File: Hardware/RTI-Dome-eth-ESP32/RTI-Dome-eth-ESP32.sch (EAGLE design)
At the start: 96 parts, among them IC1 LM2675MX-5.0_NOPB, IC2 24LC64T-I/SN, IC8 REG1117-3.3V, J1 691313510003, J10 691313510002, J11 691313510002, J12 691313510002, J2 XT60PW-M, J3 691313510003, J4 691313510003, J6 691313510003, J7 691313510003, J8 691313510002, J9 691313510002, T1 MMBT3904LT1, T2 MMBT3904LT1, T3 MMBT3904LT1, U1 W5500, U2 ESP32-DevKitC-32UE, X9 J1011F01PNL

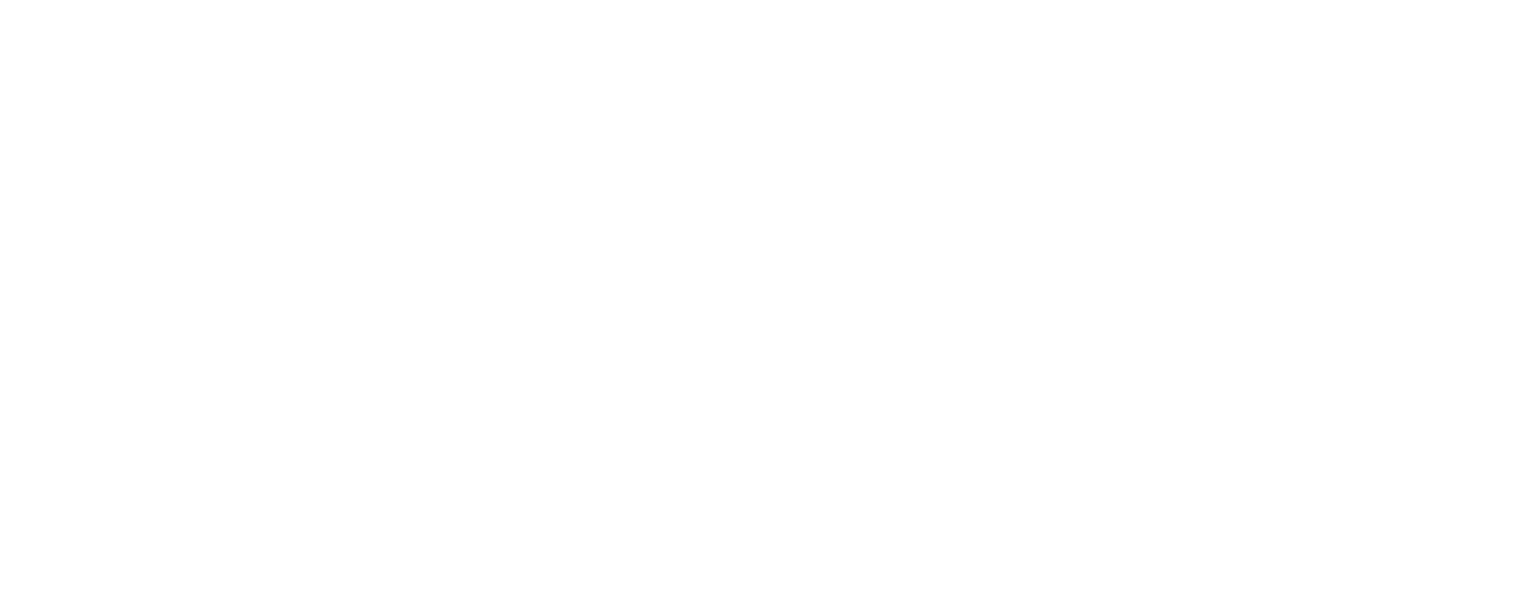
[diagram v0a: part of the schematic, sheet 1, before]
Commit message: Changing 5V circuit
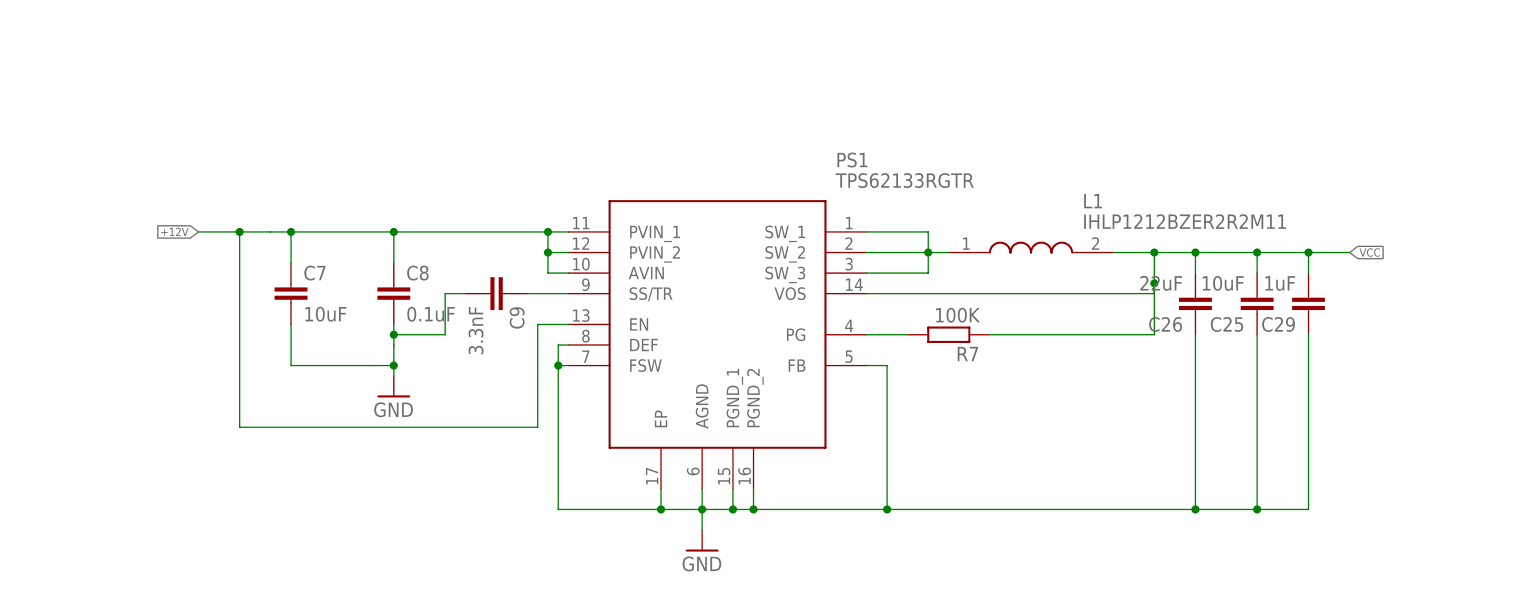
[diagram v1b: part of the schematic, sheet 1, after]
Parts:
- added C25: 10uF, rcl:C-EUC0805
- added C26: 22uF, rcl:C-EUC0805
- added C29: 1uF, rcl:C-EUC0805
- added C7: 10uF, rcl:C-EUC1206
- added C8: 0.1uF, rcl:C-EUC1206
- added C9: 3.3nF, rcl:C-EUC0805
- added L1: IHLP1212BZER2R2M11, samacsys:IHLP1212BZER2R2M11
- added PS1: TPS62133RGTR, samacsys:TPS62133RGTR
- added R7: 100K, rcl:R-EU_R0603
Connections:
- new net PG: PS1.PG, R7.2
- new net SS/TR: C9.1, PS1.SS/TR
- new net SW: L1.1, PS1.SW_1, PS1.SW_2, PS1.SW_3
- net +12V: now also C7.1, C8.1, PS1.AVIN, PS1.EN, PS1.PVIN_1, PS1.PVIN_2
- net GND: now also C25.1, C26.1, C29.1, C7.2, C8.2, C9.2, PS1.AGND, PS1.DEF, PS1.EP, PS1.FB, PS1.FSW, PS1.PGND_1, PS1.PGND_2
- net VCC: now also C25.2, C26.2, C29.2, L1.2, PS1.VOS, R7.1

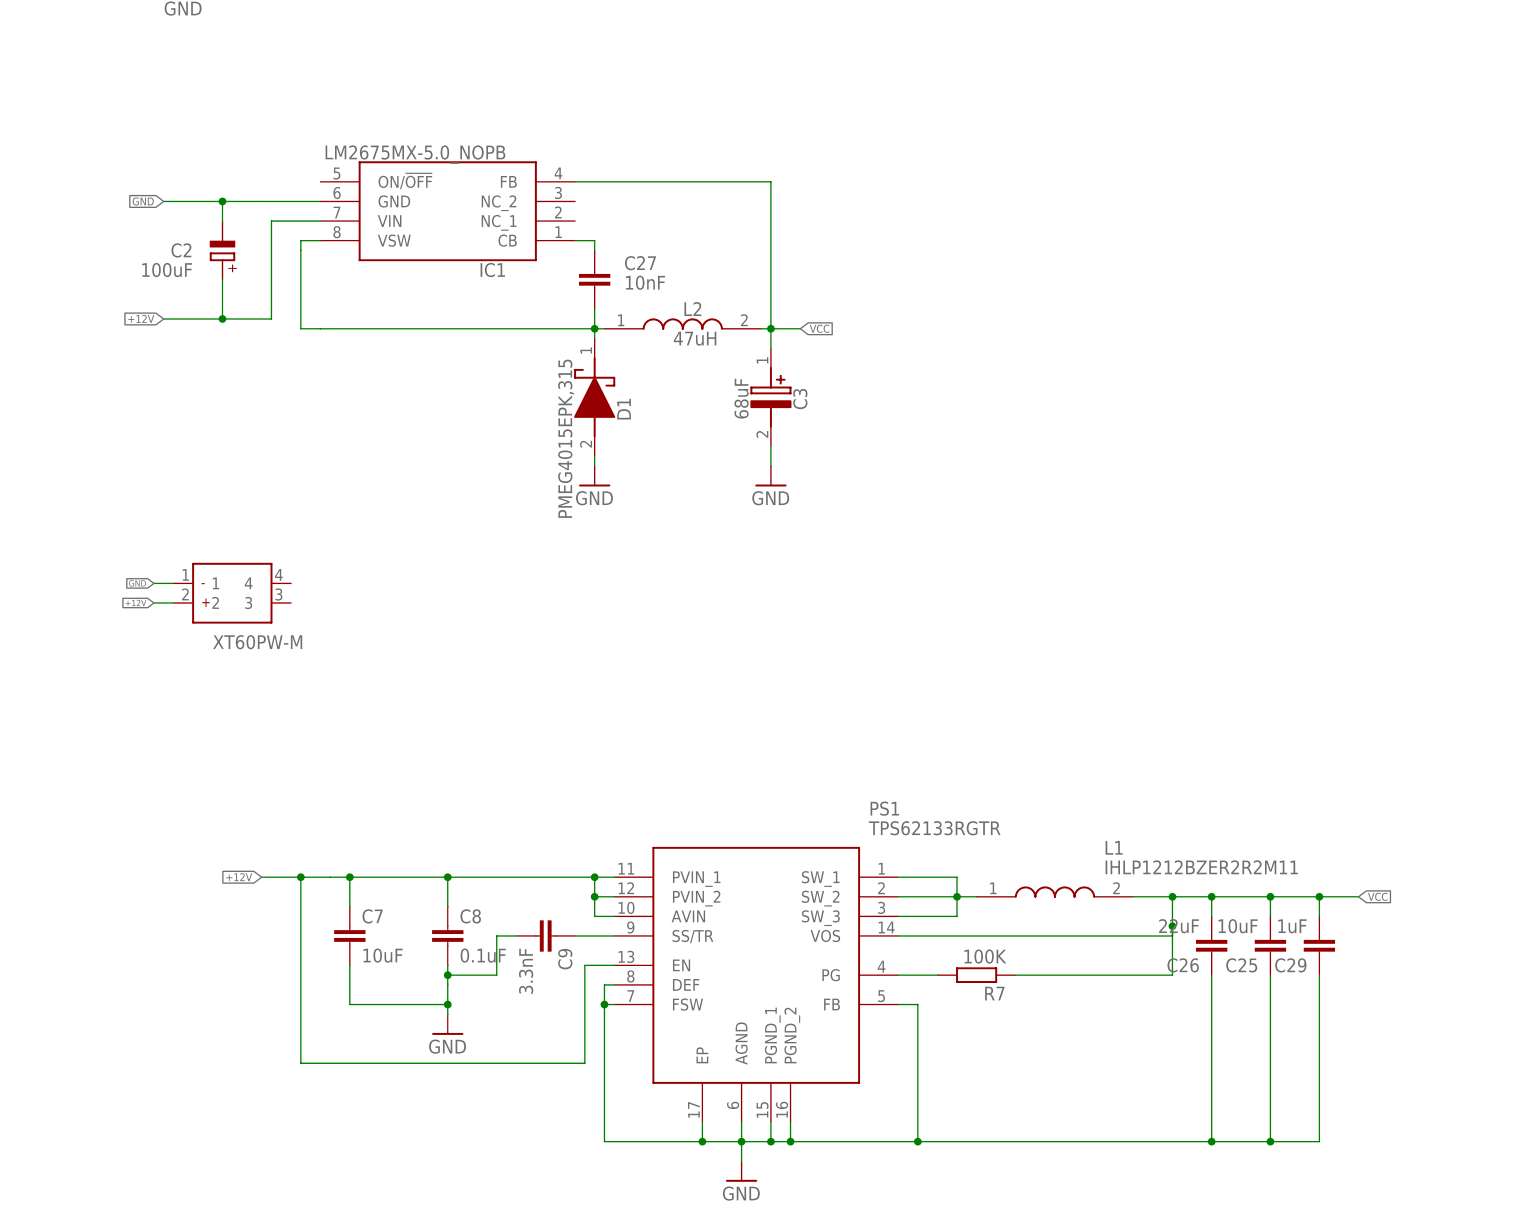
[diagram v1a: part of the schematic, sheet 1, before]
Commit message: New 5V circuit routed
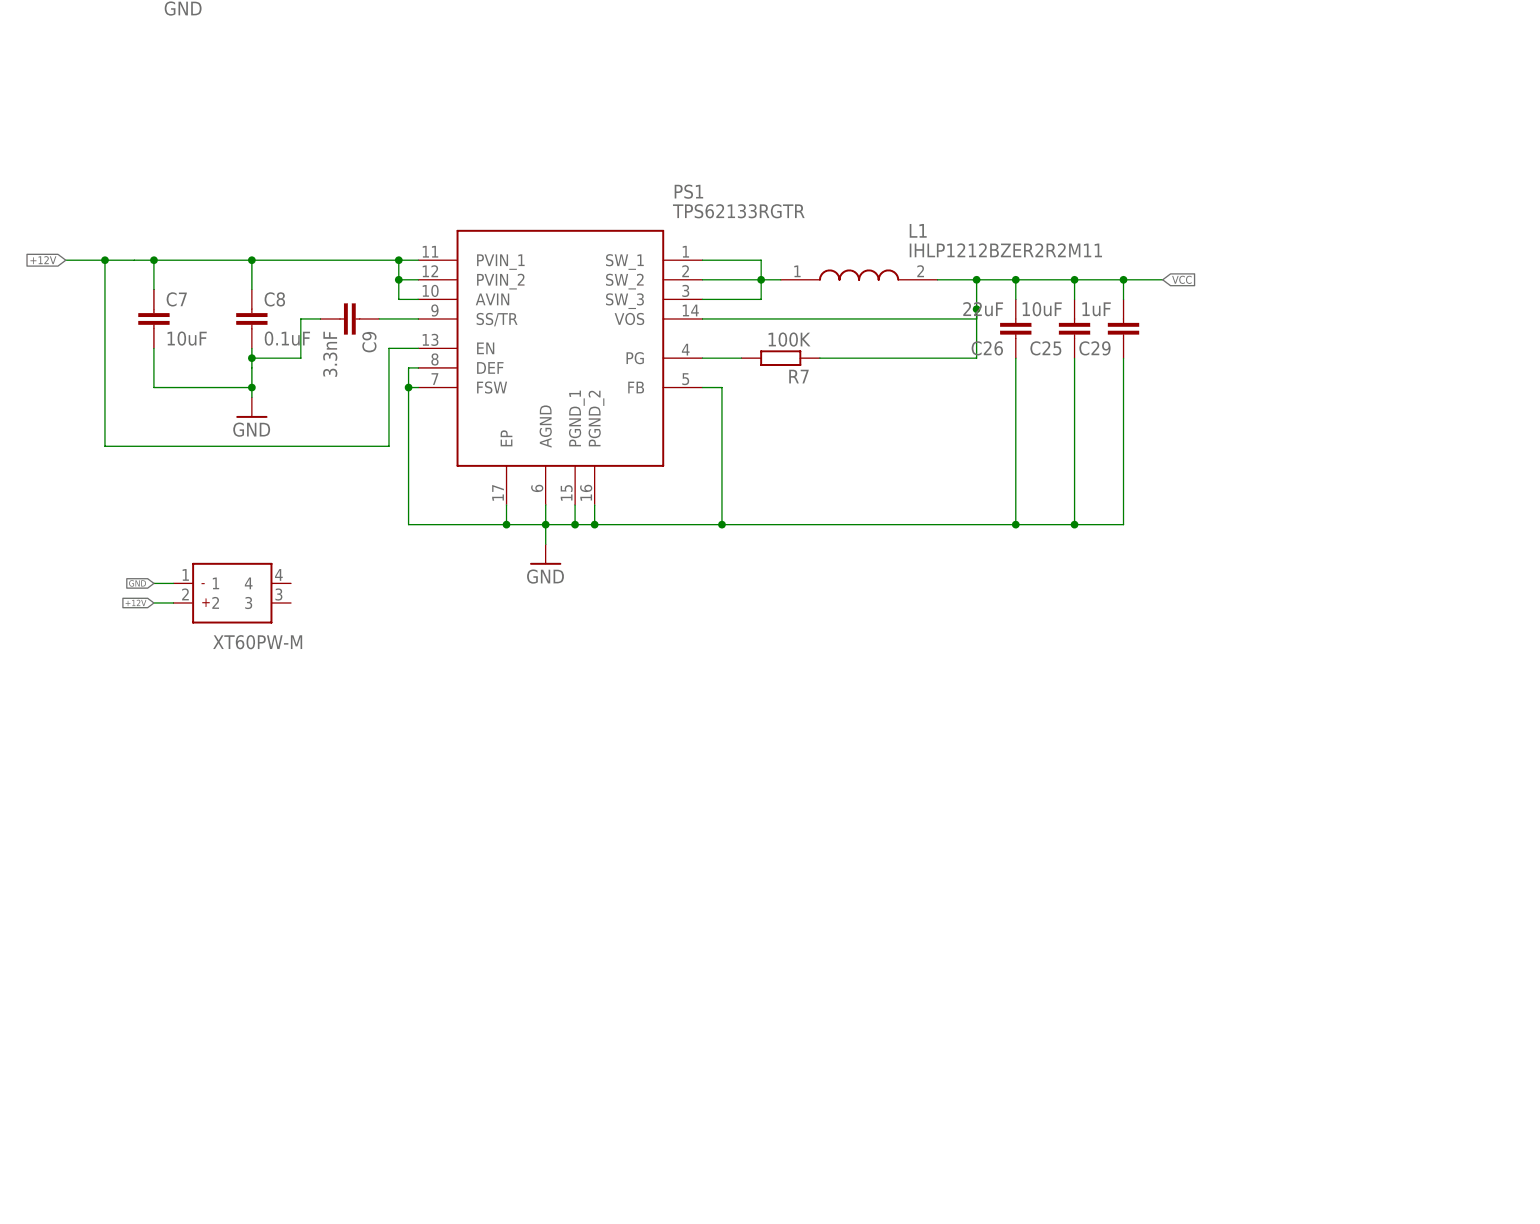
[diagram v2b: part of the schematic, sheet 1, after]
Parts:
- removed C2: 100uF, rcl:CPOL-EUUD-6,3X7,7
- removed C27: 10nF, rcl:C-EUC0805
- removed C3: 68uF, samacsys:EEE-FP1C680AL
- removed D1: PMEG4015EPK,315, samacsys:PMEG4015EPK,315
- removed IC1: LM2675MX-5.0_NOPB, samacsys:LM2675MX-5.0_NOPB
- removed L2: 47uH, samacsys:784777470
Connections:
- removed net N$2: C27.1, IC1.CB
- removed net SWV: C27.2, D1.K, IC1.VSW, L2.1
- net +12V: no longer C2.+, IC1.VIN
- net GND: no longer C2.-, C3.-, D1.A, IC1.GND
- net VCC: no longer C3.+, IC1.FB, L2.2
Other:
- moved on the sheet: C25, C26, C29, C7, C8, C9, L1, PS1, R7

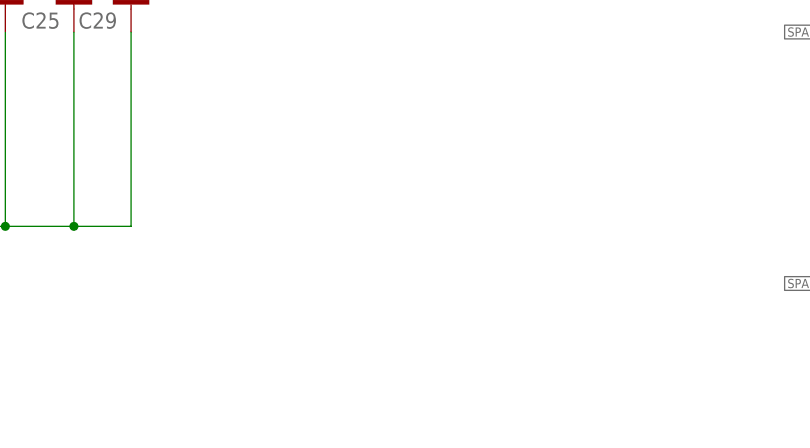
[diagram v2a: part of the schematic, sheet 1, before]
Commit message: Better 12V input filtering
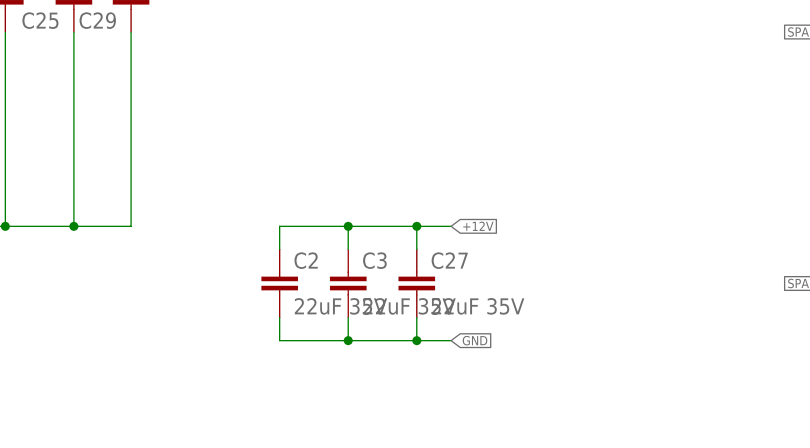
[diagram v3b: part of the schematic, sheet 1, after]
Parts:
- added C2, C27, C3: 22uF 35V, rcl:C-EUC1206
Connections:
- net +12V: now also C2.1, C27.1, C3.1
- net GND: now also C2.2, C27.2, C3.2
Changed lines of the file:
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@@
 <part name="C29" library="rcl" library_urn="urn:adsk.eagle:library:334" deviceset="C-EU" device="C0805" package3d_urn="urn:adsk.eagle:package:23617/2" value="1uF"/>
 <part name="C26" library="rcl" library_urn="urn:adsk.eagle:library:334" deviceset="C-EU" device="C0805" package3d_urn="urn:adsk.eagle:package:23617/2" value="22uF"/>
+<part name="C2" library="rcl" library_urn="urn:adsk.eagle:library:334" deviceset="C-EU" device="C1206" package3d_urn="urn:adsk.eagle:package:23618/2" value="22uF 35V"/>
+<part name="C3" library="rcl" library_urn="urn:adsk.eagle:library:334" deviceset="C-EU" device="C1206" package3d_urn="urn:adsk.eagle:package:23618/2" value="22uF 35V"/>
+<part name="C27" library="rcl" library_urn="urn:adsk.eagle:library:334" deviceset="C-EU" device="C1206" package3d_urn="urn:adsk.eagle:package:23618/2" value="22uF 35V"/>
 </parts>
 <sheets>
@@
 <attribute name="NAME" x="136.906" y="51.689" size="1.778" layer="95" rot="R180"/>
 <attribute name="VALUE" x="136.906" y="56.769" size="1.778" layer="96" rot="R180"/>
+</instance>
+<instance part="C2" gate="G$1" x="168.91" y="22.86" smashed="yes">
+<attribute name="NAME" x="170.434" y="23.241" size="1.778" layer="95"/>
+<attribute name="VALUE" x="170.434" y="18.161" size="1.778" layer="96"/>
+</instance>
+<instance part="C3" gate="G$1" x="176.53" y="22.86" smashed="yes">
+<attribute name="NAME" x="178.054" y="23.241" size="1.778" layer="95"/>
+<attribute name="VALUE" x="178.054" y="18.161" size="1.778" layer="96"/>
+</instance>
+<instance part="C27" gate="G$1" x="184.15" y="22.86" smashed="yes">
+<attribute name="NAME" x="185.674" y="23.241" size="1.778" layer="95"/>
+<attribute name="VALUE" x="185.674" y="18.161" size="1.778" layer="96"/>
 </instance>
 </instances>
@@
 <pinref part="C26" gate="G$1" pin="1"/>
 </segment>
+<segment>
+<pinref part="C2" gate="G$1" pin="2"/>
+<wire x1="168.91" y1="17.78" x2="168.91" y2="15.24" width="0.1524" layer="91"/>
+<wire x1="168.91" y1="15.24" x2="176.53" y2="15.24" width="0.1524" layer="91"/>
+<pinref part="C27" gate="G$1" pin="2"/>
+<wire x1="176.53" y1="15.24" x2="184.15" y2="15.24" width="0.1524" layer="91"/>
+<wire x1="184.15" y1="15.24" x2="184.15" y2="17.78" width="0.1524" layer="91"/>
+<pinref part="C3" gate="G$1" pin="2"/>
+<wire x1="176.53" y1="15.24" x2="176.53" y2="17.78" width="0.1524" layer="91"/>
+<junction x="176.53" y="15.24"/>
+<wire x1="187.96" y1="15.24" x2="184.15" y2="15.24" width="0.1524" layer="91"/>
+<junction x="184.15" y="15.24"/>
+<label x="187.96" y="15.24" size="1.016" layer="95" xref="yes"/>
+</segment>
 </net>
 <net name="+12V" class="1">
@@
 <pinref part="C8" gate="G$1" pin="1"/>
 </segment>
+<segment>
+<pinref part="C2" gate="G$1" pin="1"/>
+<wire x1="168.91" y1="25.4" x2="168.91" y2="27.94" width="0.1524" layer="91"/>
+<pinref part="C27" gate="G$1" pin="1"/>
+<wire x1="168.91" y1="27.94" x2="176.53" y2="27.94" width="0.1524" layer="91"/>
+<wire x1="176.53" y1="27.94" x2="184.15" y2="27.94" width="0.1524" layer="91"/>
+<wire x1="184.15" y1="27.94" x2="184.15" y2="25.4" width="0.1524" layer="91"/>
+<pinref part="C3" gate="G$1" pin="1"/>
+<wire x1="176.53" y1="25.4" x2="176.53" y2="27.94" width="0.1524" layer="91"/>
+<junction x="176.53" y="27.94"/>
+<wire x1="187.96" y1="27.94" x2="184.15" y2="27.94" width="0.1524" layer="91"/>
+<junction x="184.15" y="27.94"/>
+<label x="187.96" y="27.94" size="1.016" layer="95" xref="yes"/>
+</segment>
 </net>

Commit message: Re-export board from Fusion
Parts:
- JP1: value (none) -> 3PIN_Header; LCSC_PART (none) -> C19190477
